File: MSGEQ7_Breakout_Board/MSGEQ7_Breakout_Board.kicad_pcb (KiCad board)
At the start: 2 copper layers, 44.4 x 25.4 mm, 18 parts, among them J1 BREAKOUT_BOARD_HEADER, J2 STEREO_MINI_JACK, U1 MSGEQ7

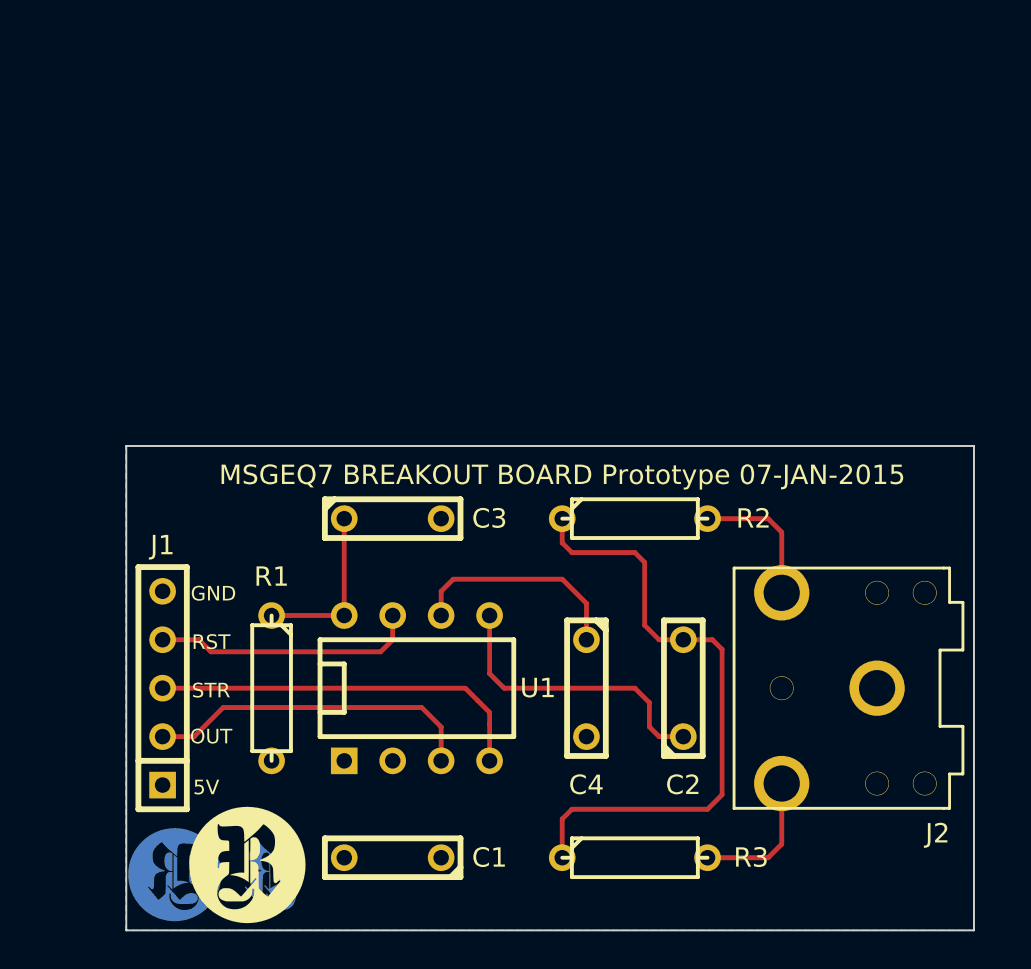
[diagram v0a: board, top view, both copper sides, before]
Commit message: All Design Files Updated to KiCad v4.0.0_RC1
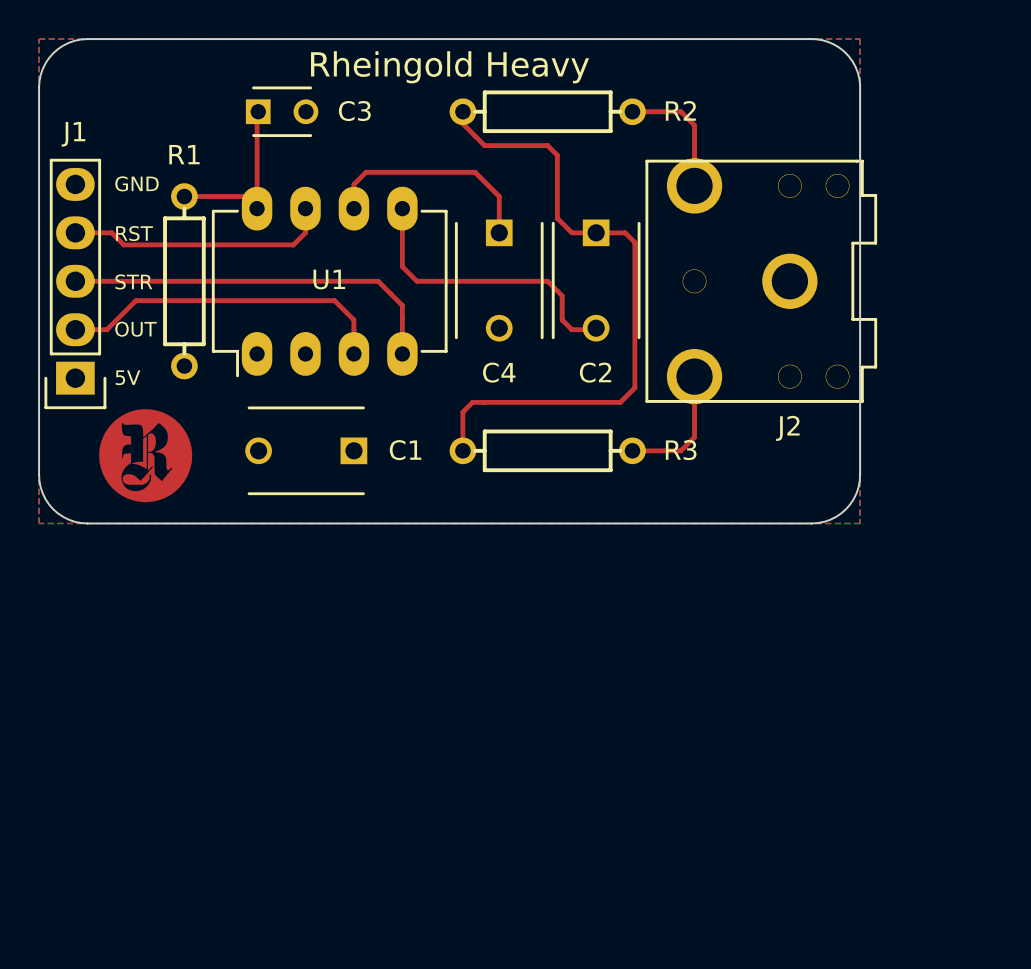
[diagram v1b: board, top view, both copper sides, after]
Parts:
- removed the VAL at (233.2, 171.1)
- removed the VAL at (227.3, 172.2)
- removed the VAL at (194.3, 172.3) (x2)
- removed the VAL at (199.4, 172.3) (x3)
- removed the VAL at (198.1, 171.8)
- added VAL: REF, Logo_RH_Circle_R__F.Cu_.2in, F.Cu at (192.8, 150.4)
- added VAL: REF, Logo_RH_Circle_R__F.Mask_.2in, F.Cu at (192.8, 150.4)
- added VAL: REF, Logo_RH_Circle_R_B.SilkS_.750in_flipped, F.Cu at (208.8, 141.2)
- C1, C2, C4: footprint C2 -> Capacitors_ThroughHole:C_Disc_D6_P5
- C3: footprint C2 -> Capacitors_ThroughHole:C_Disc_D3_P2.5
- J1: footprint SIL-5 -> Pin_Headers:Pin_Header_Straight_1x05
- R1, R2, R3: footprint R3 -> Project_Footprints:PTH_Resistor
- U1: footprint DIP-8__300 -> Housings_DIP:DIP-8_W7.62mm_LongPads
- moved C2 24.3 mm to (216.4, 138.7), turned to 270 degrees
- moved C4 24.3 mm to (211.3, 138.7)
- moved C3 22.5 mm to (198.7, 132.3)
- moved J2 21.8 mm to (226.6, 141.2)
- moved R1 21.8 mm to (194.8, 141.2)
- moved R2 21.8 mm to (213.9, 132.3)
- moved R3 21.8 mm to (213.9, 150.1)
- moved C1 21.4 mm to (203.7, 150.1)
- moved U1 19.4 mm to (198.6, 145.0), turned to 90 degrees
- moved J1 15.7 mm to (189.1, 146.3), turned to 180 degrees
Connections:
- C2 pad 1: N-000003 -> Net-(C2-Pad1)
- C2 pad 2: N-000004 -> Net-(C2-Pad2)
- R2 pad 1: N-000004 -> Net-(C2-Pad1)
- R3 pad 1: N-000004 -> Net-(C2-Pad1)
- U1 pad 5: N-000003 -> Net-(C2-Pad2)
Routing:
- net Net-(C2-Pad1): track 0.00 -> 33.4 mm
- net N-000004: track 32.5 -> 0.00 mm
- net Net-(C2-Pad2): track 0.00 -> 15.3 mm
- net N-000003: track 15.3 -> 0.00 mm
- net Net-(J2-Pad3): track 7.36 -> 6.73 mm
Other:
- board size 44.4 x 25.4 mm -> 43.1 x 25.4 mm
- board text added: "Rheingold Heavy"
- board text added: "Rheingold Heavy MSGEQ7 Breakout Board"
- board text removed: "100mil"
- board text removed: "200mil"
- board text removed: "MSGEQ7 BREAKOUT BOARD Prototype 07-JAN-2015"
